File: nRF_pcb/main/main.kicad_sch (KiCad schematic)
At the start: 6 parts, among them U1 XIAO-nRF52840-SMD, U2 SSD1306

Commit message: WIP
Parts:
- added J1: SWD breakout, diy_recreations:SWD breakout, symbol Connector:Conn_01x04_Socket
- BAT+1: renamed from BAT+; footprint (none) -> diy_recreations:Battery Header
- U1: footprint Seeed_Studio_XIAO_Series:XIAO-nRF52840-SMD -> XIAO_Series_Footprints:XIAO-nRF52840-SMD
- U2: footprint (none) -> diy_recreations:SSD1306
- U3: value ~ -> SM5308 LiPo; footprint (none) -> diy_recreations:SM5308 LiPo charger
- U4: value ~ -> BE-280; footprint (none) -> diy_recreations:BE-280 GPS
- U5: value ~ -> SD Breakout; footprint (none) -> diy_recreations:Adafruit SD Breakout
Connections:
- net +5V: now also U3.1 (5V); no longer U3. (+BAT)
- net GND: now also U3.2 (GND); no longer U3. (+BAT)
- net at BAT+1.1 (Pin_1): now also U3.5 (+BAT); no longer U3. (+BAT)
- net at BAT+1.2 (Pin_2): now also U3.4 (-BAT); no longer U3. (+BAT)
- net at U1.1 (P0.02_A0_D0): now also U3.3 (KEY); no longer U3. (+BAT)
- net at U1.24 (SWDIO): now also J1.1 (Pin_1)
- net at U1.25 (SWCLK): now also J1.2 (Pin_2)
- net at U1.26 (RESET): now also J1.3 (Pin_3)
- net at U1.27 (GND): now also J1.4 (Pin_4)
- no-connect marks 0 -> 19
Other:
- moved on the sheet: U2

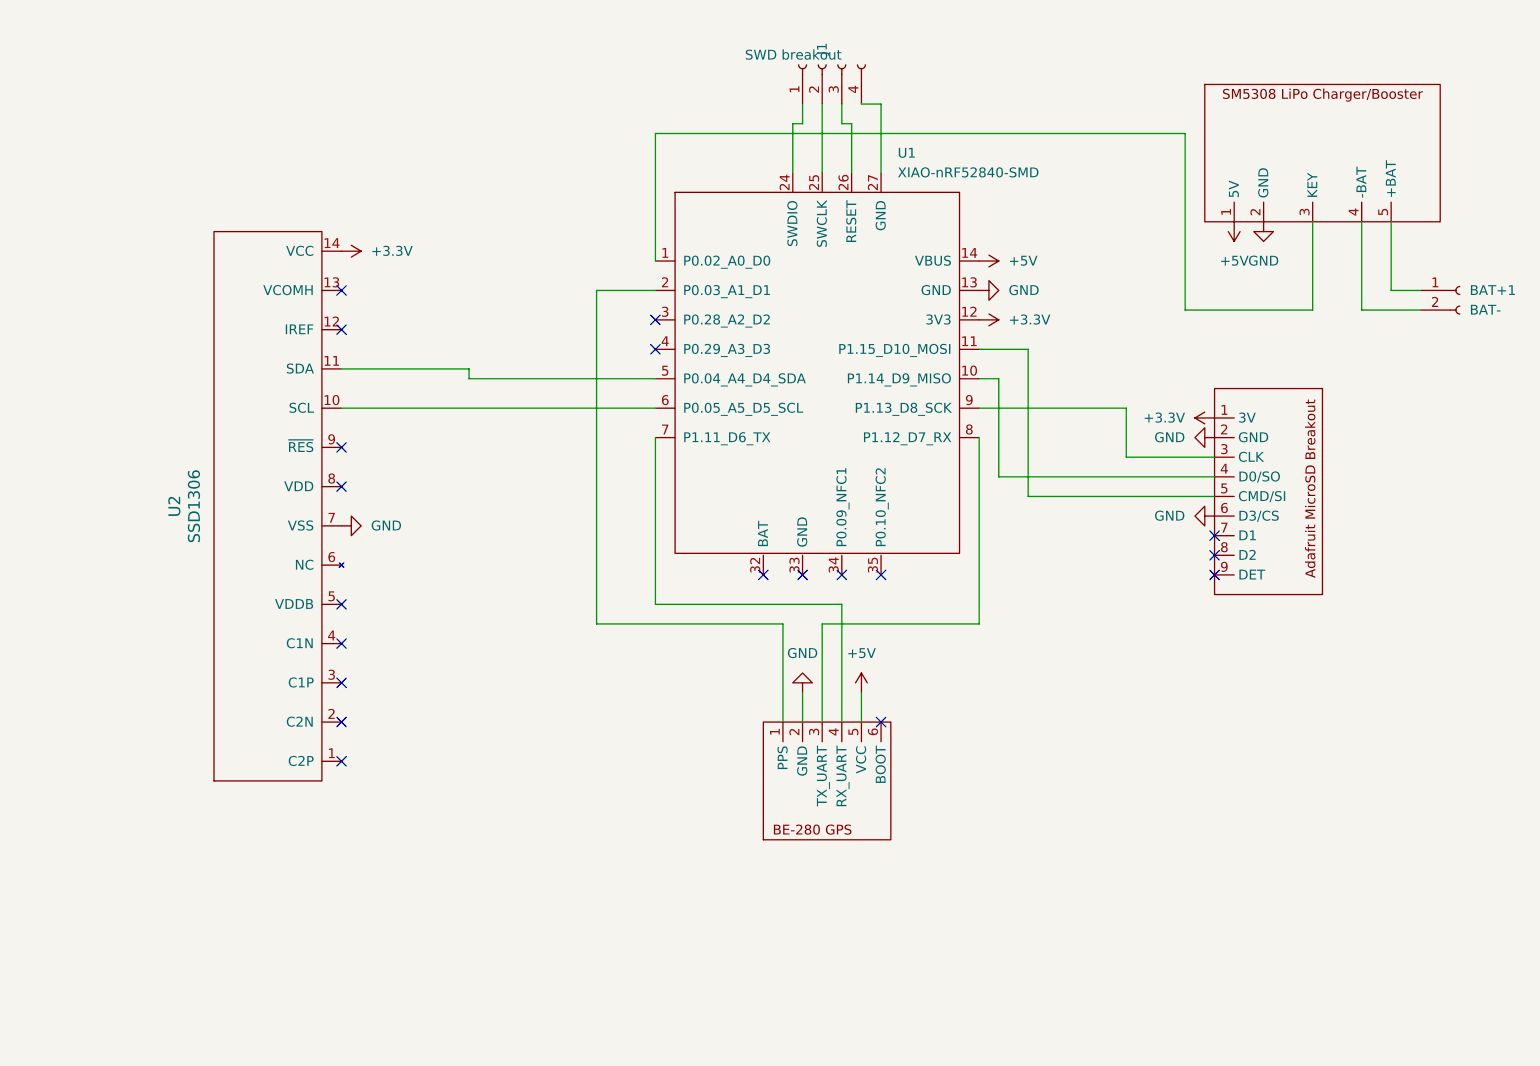
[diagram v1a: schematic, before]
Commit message: Refactor wires to labels
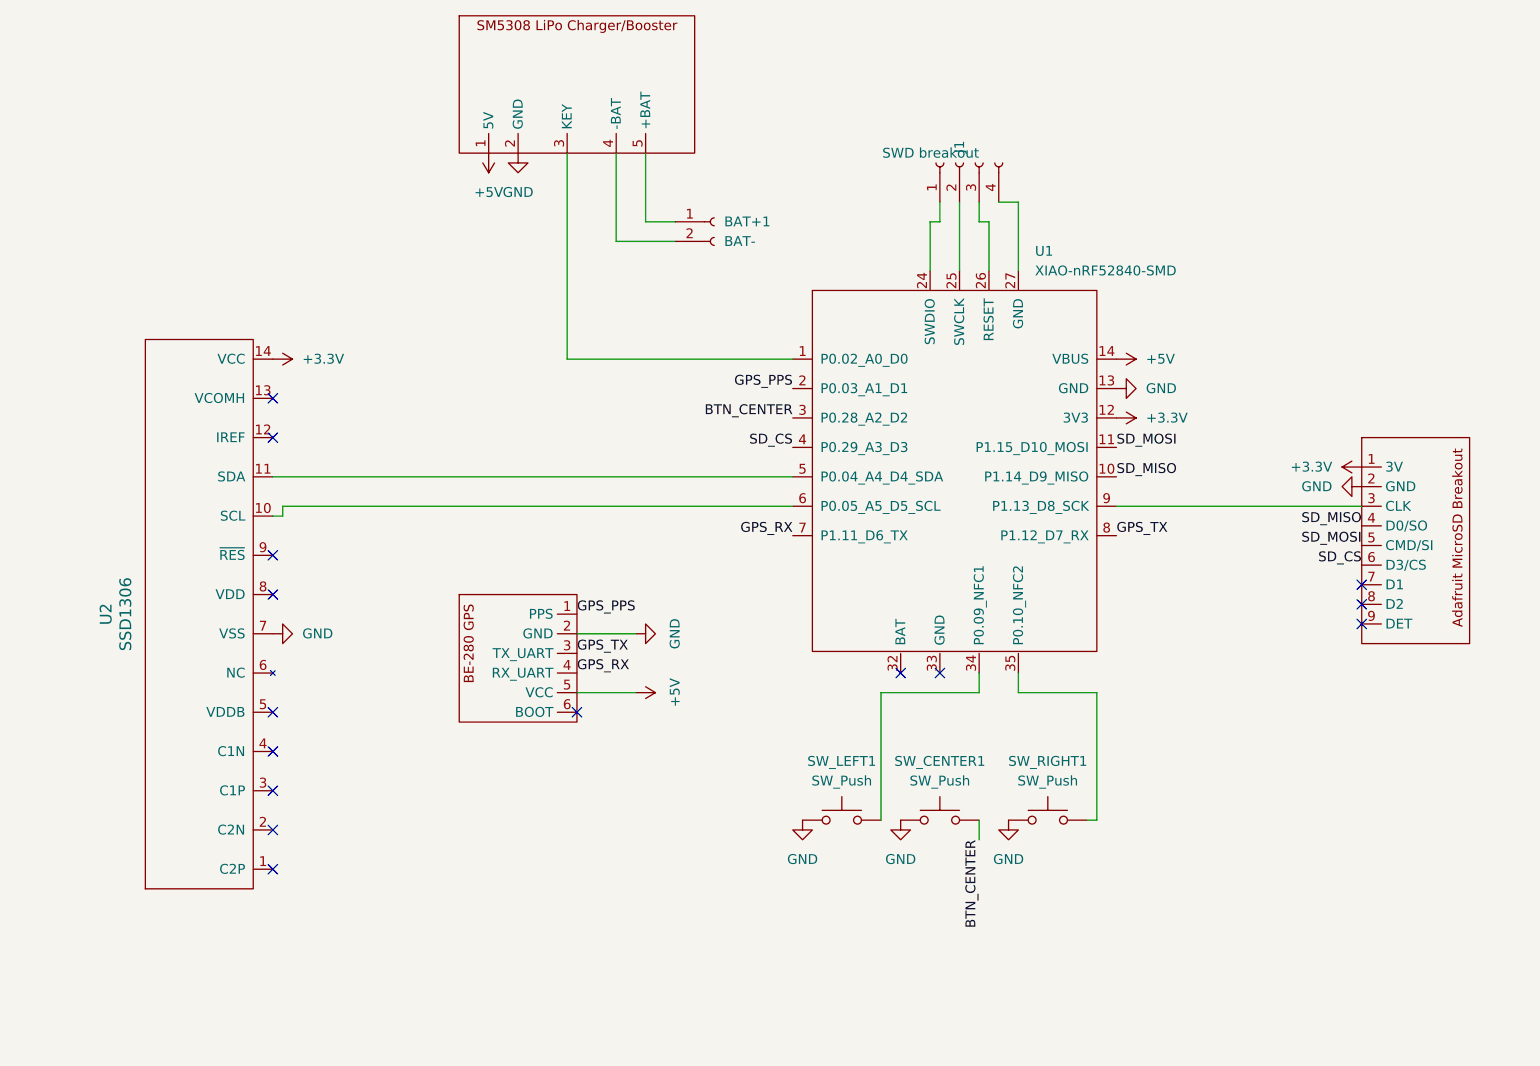
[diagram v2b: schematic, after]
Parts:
- added SW_CENTER1, SW_LEFT1, SW_RIGHT1: SW_Push, symbol Switch:SW_Push
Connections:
- net GND: now also SW_CENTER1.1, SW_LEFT1.1, SW_RIGHT1.1; no longer U5.6 (D3/CS)
- net GPS_PPS: now reaches U1.2 (P0.03_A1_D1), U4.1 (PPS)
- net GPS_TX: now reaches U1.8 (P1.12_D7_RX), U4.3 (TX_UART)
- net GPS_RX: now reaches U1.7 (P1.11_D6_TX), U4.4 (RX_UART)
- net SD_MISO: now reaches U1.10 (P1.14_D9_MISO), U5.4 (D0/SO)
- net SD_MOSI: now reaches U1.11 (P1.15_D10_MOSI), U5.5 (CMD/SI)
- net BTN_CENTER: now reaches U1.3 (P0.28_A2_D2)
- net BTN_CENTER: now also SW_CENTER1.2
- net at U1.34 (P0.09_NFC1): now also SW_LEFT1.2
- net at U1.35 (P0.10_NFC2): now also SW_RIGHT1.2
- net SD_CS: now reaches U1.4 (P0.29_A3_D3)
- net SD_CS: now also U5.6 (D3/CS)
- no-connect marks 19 -> 15
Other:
- moved on the sheet: BAT+1, J1, U1, U2

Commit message: Update PCB
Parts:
- SW_CENTER1: footprint (none) -> diy_recreations:Button Center
- SW_LEFT1: footprint (none) -> diy_recreations:Button Left
- SW_RIGHT1: footprint (none) -> diy_recreations:Button Right
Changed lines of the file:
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@@
 			)
 		)
-		(property "Footprint" ""
+		(property "Footprint" "diy_recreations:Button Center"
 			(at 138.43 113.03 0)
 			(effects
@@
 			)
 		)
-		(property "Footprint" ""
+		(property "Footprint" "diy_recreations:Button Left"
 			(at 125.73 113.03 0)
 			(effects
@@
 			)
 		)
-		(property "Footprint" ""
+		(property "Footprint" "diy_recreations:Button Right"
 			(at 152.4 113.03 0)
 			(effects

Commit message: Refactor to 3.3V only architecture
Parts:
- removed U3: SM5308 LiPo, diy_recreations:SM5308 LiPo charger, symbol diy:SM5308_LiPo_Charger
- U1: footprint XIAO_Series_Footprints:XIAO-nRF52840-SMD -> XIAO_Series_Footprints:XIAO-nRF52840-DIP
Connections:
- net +3.3V: now also U4.5 (VCC)
- net at BAT+1.1 (Pin_1): now also U1.32 (BAT)
- net at BAT+1.2 (Pin_2): now also U1.33 (GND)
- net +5V: no longer names the net of U1.14 (VBUS)
- net +5V: no longer U4.5 (VCC)
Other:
- moved on the sheet: BAT+1, SW_CENTER1, SW_LEFT1, SW_RIGHT1

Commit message: Add 3V3 rail toggle
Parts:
- added Q1: AO3401A, Package_TO_SOT_SMD:SOT-23, symbol Transistor_FET:AO3401A
- added R1: 100k, symbol Device:R
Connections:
- net +3.3V: now also Q1.2 (S); no longer U1.12 (3V3)
- net 3V3_ENABLE: now reaches U1.1 (P0.02_A0_D0)
- net 3V3_ENABLE: now also Q1.1 (G), R1.1
- new net: Q1.3 (D), R1.2, U1.12 (3V3)
- no-connect marks 15 -> 14
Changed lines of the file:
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@@
 		(date "2026-02-26")
+	)
+	(junction
+		(at 180.34 55.88)
+		(diameter 0)
+		(color 0 0 0 0)
+	)
+	(junction
+		(at 175.26 66.04)
+		(diameter 0)
+		(color 0 0 0 0)
 	)
 	(no_connect
@@
 	)
 	(no_connect
-		(at 119.38 58.42)
-	)
-	(no_connect
 		(at 91.44 104.14)
 	)
@@
 	(wire
 		(pts
+			(xy 180.34 55.88) (xy 184.15 55.88)
+		)
+		(stroke
+			(width 0)
+			(type default)
+		)
+	)
+	(wire
+		(pts
 			(xy 148.59 115.57) (xy 148.59 99.06)
 		)
@@
 	(wire
 		(pts
+			(xy 175.26 45.72) (xy 175.26 66.04)
+		)
+		(stroke
+			(width 0)
+			(type default)
+		)
+	)
+	(wire
+		(pts
 			(xy 144.78 46.99) (xy 144.78 40.64)
 		)
@@
 	(wire
 		(pts
+			(xy 180.34 53.34) (xy 180.34 55.88)
+		)
+		(stroke
+			(width 0)
+			(type default)
+		)
+	)
+	(wire
+		(pts
 			(xy 133.35 99.06) (xy 133.35 102.87)
 		)
@@
 	(wire
 		(pts
+			(xy 175.26 66.04) (xy 180.34 66.04)
+		)
+		(stroke
+			(width 0)
+			(type default)
+		)
+	)
+	(wire
+		(pts
 			(xy 161.29 77.47) (xy 193.04 77.47)
 		)
@@
 	(wire
 		(pts
+			(xy 180.34 55.88) (xy 180.34 58.42)
+		)
+		(stroke
+			(width 0)
+			(type default)
+		)
+	)
+	(wire
+		(pts
 			(xy 53.34 77.47) (xy 119.38 77.47)
 		)
@@
 		(pts
 			(xy 99.06 93.98) (xy 91.44 93.98)
+		)
+		(stroke
+			(width 0)
+			(type default)
+		)
+	)
+	(wire
+		(pts
+			(xy 161.29 66.04) (xy 175.26 66.04)
 		)
 		(stroke
@@
 		)
 	)
+	(label "3V3_ENABLE"
+		(at 119.38 58.42 180)
+		(effects
+			(font
+				(size 1.27 1.27)
+			)
+			(justify right bottom)
+		)
+	)
 	(label "SD_MOSI"
 		(at 193.04 82.55 180)
@@
 			)
 			(justify right bottom)
+		)
+	)
+	(label "3V3_ENABLE"
+		(at 184.15 55.88 0)
+		(effects
+			(font
+				(size 1.27 1.27)
+			)
+			(justify left bottom)
 		)
 	)
@@
 				(path "/0a7ddd5c-f520-487e-b759-77dfaf69ba0a"
 					(reference "SW_CENTER1")
+					(unit 1)
+				)
+			)
+		)
+	)
+	(symbol
+		(lib_id "Transistor_FET:AO3401A")
+		(at 180.34 48.26 90)
+		(unit 1)
+		(exclude_from_sim no)
+		(in_bom yes)
+		(on_board yes)
+		(dnp no)
+		(fields_autoplaced yes)
+		(property "Reference" "Q1"
+			(at 180.34 39.37 90)
+			(effects
+				(font
+					(size 1.27 1.27)
+				)
+			)
+		)
+		(property "Value" "AO3401A"
+			(at 180.34 41.91 90)
+			(effects
+				(font
+					(size 1.27 1.27)
+				)
+			)
+		)
+		(property "Footprint" "Package_TO_SOT_SMD:SOT-23"
+			(at 182.245 43.18 0)
+			(effects
+				(font
+					(size 1.27 1.27)
+					(italic yes)
+				)
+				(justify left)
+				(hide yes)
+			)
+		)
+		(property "Datasheet" "http://www.aosmd.com/pdfs/datasheet/AO3401A.pdf"
+			(at 184.15 43.18 0)
+			(effects
+				(font
+					(size 1.27 1.27)
+				)
+				(justify left)
+				(hide yes)
+			)
+		)
+		(property "Description" "-4.0A Id, -30V Vds, P-Channel MOSFET, SOT-23"
+			(at 180.34 48.26 0)
+			(effects
+				(font
+					(size 1.27 1.27)
+				)
+				(hide yes)
+			)
+		)
+		(pin "1"
+		)
+		(pin "2"
+		)
+		(pin "3"
+		)
+		(instances
+			(project ""
+				(path "/0a7ddd5c-f520-487e-b759-77dfaf69ba0a"
+					(reference "Q1")
 					(unit 1)
 				)
@@
 	)
 	(symbol
+		(lib_id "Device:R")
+		(at 180.34 62.23 0)
+		(unit 1)
+		(exclude_from_sim no)
+		(in_bom yes)
+		(on_board yes)
+		(dnp no)
+		(fields_autoplaced yes)
+		(property "Reference" "R1"
+			(at 182.88 60.9599 0)
+			(effects
+				(font
+					(size 1.27 1.27)
+				)
+				(justify left)
+			)
+		)
+		(property "Value" "100k"
+			(at 182.88 63.4999 0)
+			(effects
+				(font
+					(size 1.27 1.27)
+				)
+				(justify left)
+			)
+		)
+		(property "Footprint" ""
+			(at 178.562 62.23 90)
+			(effects
+				(font
+					(size 1.27 1.27)
+				)
+				(hide yes)
+			)
+		)
+		(property "Datasheet" "~"
+			(at 180.34 62.23 0)
+			(effects
+				(font
+					(size 1.27 1.27)
+				)
+				(hide yes)
+			)
+		)
+		(property "Description" "Resistor"
+			(at 180.34 62.23 0)
+			(effects
+				(font
+					(size 1.27 1.27)
+				)
+				(hide yes)
+			)
+		)
+		(pin "1"
+		)
+		(pin "2"
+		)
+		(instances
+			(project ""
+				(path "/0a7ddd5c-f520-487e-b759-77dfaf69ba0a"
+					(reference "R1")
+					(unit 1)
+				)
+			)
+		)
+	)
+	(symbol
 		(lib_id "power:+3.3V")
-		(at 161.29 66.04 270)
+		(at 185.42 45.72 270)
 		(unit 1)
 		(exclude_from_sim no)
@@
 		(fields_autoplaced yes)
 		(property "Reference" "#PWR08"
-			(at 157.48 66.04 0)
+			(at 181.61 45.72 0)
 			(effects
 				(font
@@
 		)
 		(property "Value" "+3.3V"
-			(at 165.1 66.0399 90)
+			(at 189.23 45.7199 90)
 			(effects
 				(font
@@
 		)
 		(property "Footprint" ""
-			(at 161.29 66.04 0)
+			(at 185.42 45.72 0)
 			(effects
 				(font
@@
 		)
 		(property "Datasheet" ""
-			(at 161.29 66.04 0)
+			(at 185.42 45.72 0)
 			(effects
 				(font
@@
 		)
 		(property "Description" "Power symbol creates a global label with name \"+3.3V\""
-			(at 161.29 66.04 0)
-			(effects
-				(font
+			(at 185.42 45.72 0)
+			(effects
+				(font
